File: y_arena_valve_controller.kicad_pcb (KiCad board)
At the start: 2 copper layers, 76.2 x 41.3 mm, 45 parts, among them P1 HEADER_02X12_SMD, SW1 SPST_SLIDE_AS

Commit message: y_arena_valve_board -> y_arena_valve_controller
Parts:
- D1, D11, D13, D15, D17, D3, D5, D7, D9: footprint y_arena_valve_board:SOD-123 -> y_arena_valve_controller:SOD-123
- D10, D12, D14, D16, D18, D2, D4, D6, D8: footprint y_arena_valve_board:LED0805 -> y_arena_valve_controller:LED0805
- FID1, FID2, FID3, FID4: footprint y_arena_valve_board:FIDUCIAL -> y_arena_valve_controller:FIDUCIAL
- MH1, MH2, MH3: footprint y_arena_valve_board:MOUNTING_HOLE_4-40 -> y_arena_valve_controller:MOUNTING_HOLE_4-40
- P1: footprint y_arena_valve_board:HEADER_02x12_SMD -> y_arena_valve_controller:HEADER_02x12_SMD
- R1, R2, R3, R4, R5, R6, R7, R8, R9: footprint y_arena_valve_board:SM0805 -> y_arena_valve_controller:SM0805
- S1, S2, S3, S4, S5, S6, S7, S8, S9: footprint y_arena_valve_board:LEECO_LHDB -> y_arena_valve_controller:LEECO_LHDB
- SW1: footprint y_arena_valve_board:SPST_SLIDE_AS -> y_arena_valve_controller:SPST_SLIDE_AS

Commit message: First draft of schematic
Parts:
- removed P1: HEADER_02X12_SMD, y_arena_valve_controller:HEADER_02x12_SMD
- added C1: 10uF, y_arena_valve_controller:SM0805, F.Cu at (84.9, -20.0)
- added C2: 10uF, y_arena_valve_controller:SM0805, F.Cu at (111.6, -46.6)
- added C3: 0.1uF, power_switches:SM0805, F.Cu at (154.2, -46.6)
- added C4: 0.1uF, power_switches:SM0805, F.Cu at (154.2, -26.4)
- added D19: diode_low_rev_current, valve_with_led:SOD-123, F.Cu at (66.9, -5.98)
- added D20: LED_GRN, valve_with_led:LED0805, F.Cu at (70.8, -5.34)
- added R10: 499, valve_with_led:SM0805, F.Cu at (73.4, -5.38)
- added REG1: CONV_DC_DC_5VIN_12VOUT, y_arena_valve_controller:DC_DC_CONV_SKM10_DKM10, F.Cu at (115.6, 116.8)
- added TEENSY1: TEENSY_4.0, y_arena_valve_controller:TEENSY_4.0, F.Cu at (77.5, 116.8)
- added U1: TLE7230R, power_switches:PG-DSO-36, F.Cu at (144.0, -40.6)
- added U2: TLE7230R, power_switches:PG-DSO-36, F.Cu at (144.0, -20.4)
- D10, D12, D14, D16, D18, D4, D6, D8: footprint y_arena_valve_controller:LED0805 -> valve_with_led:LED0805
- D11, D13, D15, D17, D3, D5, D7, D9: footprint y_arena_valve_controller:SOD-123 -> valve_with_led:SOD-123
- R2, R3, R4, R5, R6, R7, R8, R9: footprint y_arena_valve_controller:SM0805 -> valve_with_led:SM0805
- S1, S2, S3, S4, S5, S6, S7, S8, S9: footprint y_arena_valve_controller:LEECO_LHDB -> valve_with_led:LEECO_LHDB
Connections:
- D10 pad 2: /VALVE_4 -> /VALVE_3
- D12 pad 2: /VALVE_5 -> /VALVE_4
- D14 pad 2: /VALVE_6 -> /VALVE_5
- D16 pad 2: /VALVE_7 -> /VALVE_6
- D18 pad 2: /VALVE_8 -> /VALVE_7
- D2 pad 2: /VALVE_0 -> GND
- D4 pad 2: /VALVE_1 -> /VALVE_0
- D6 pad 2: /VALVE_2 -> /VALVE_1
- D8 pad 2: /VALVE_3 -> /VALVE_2

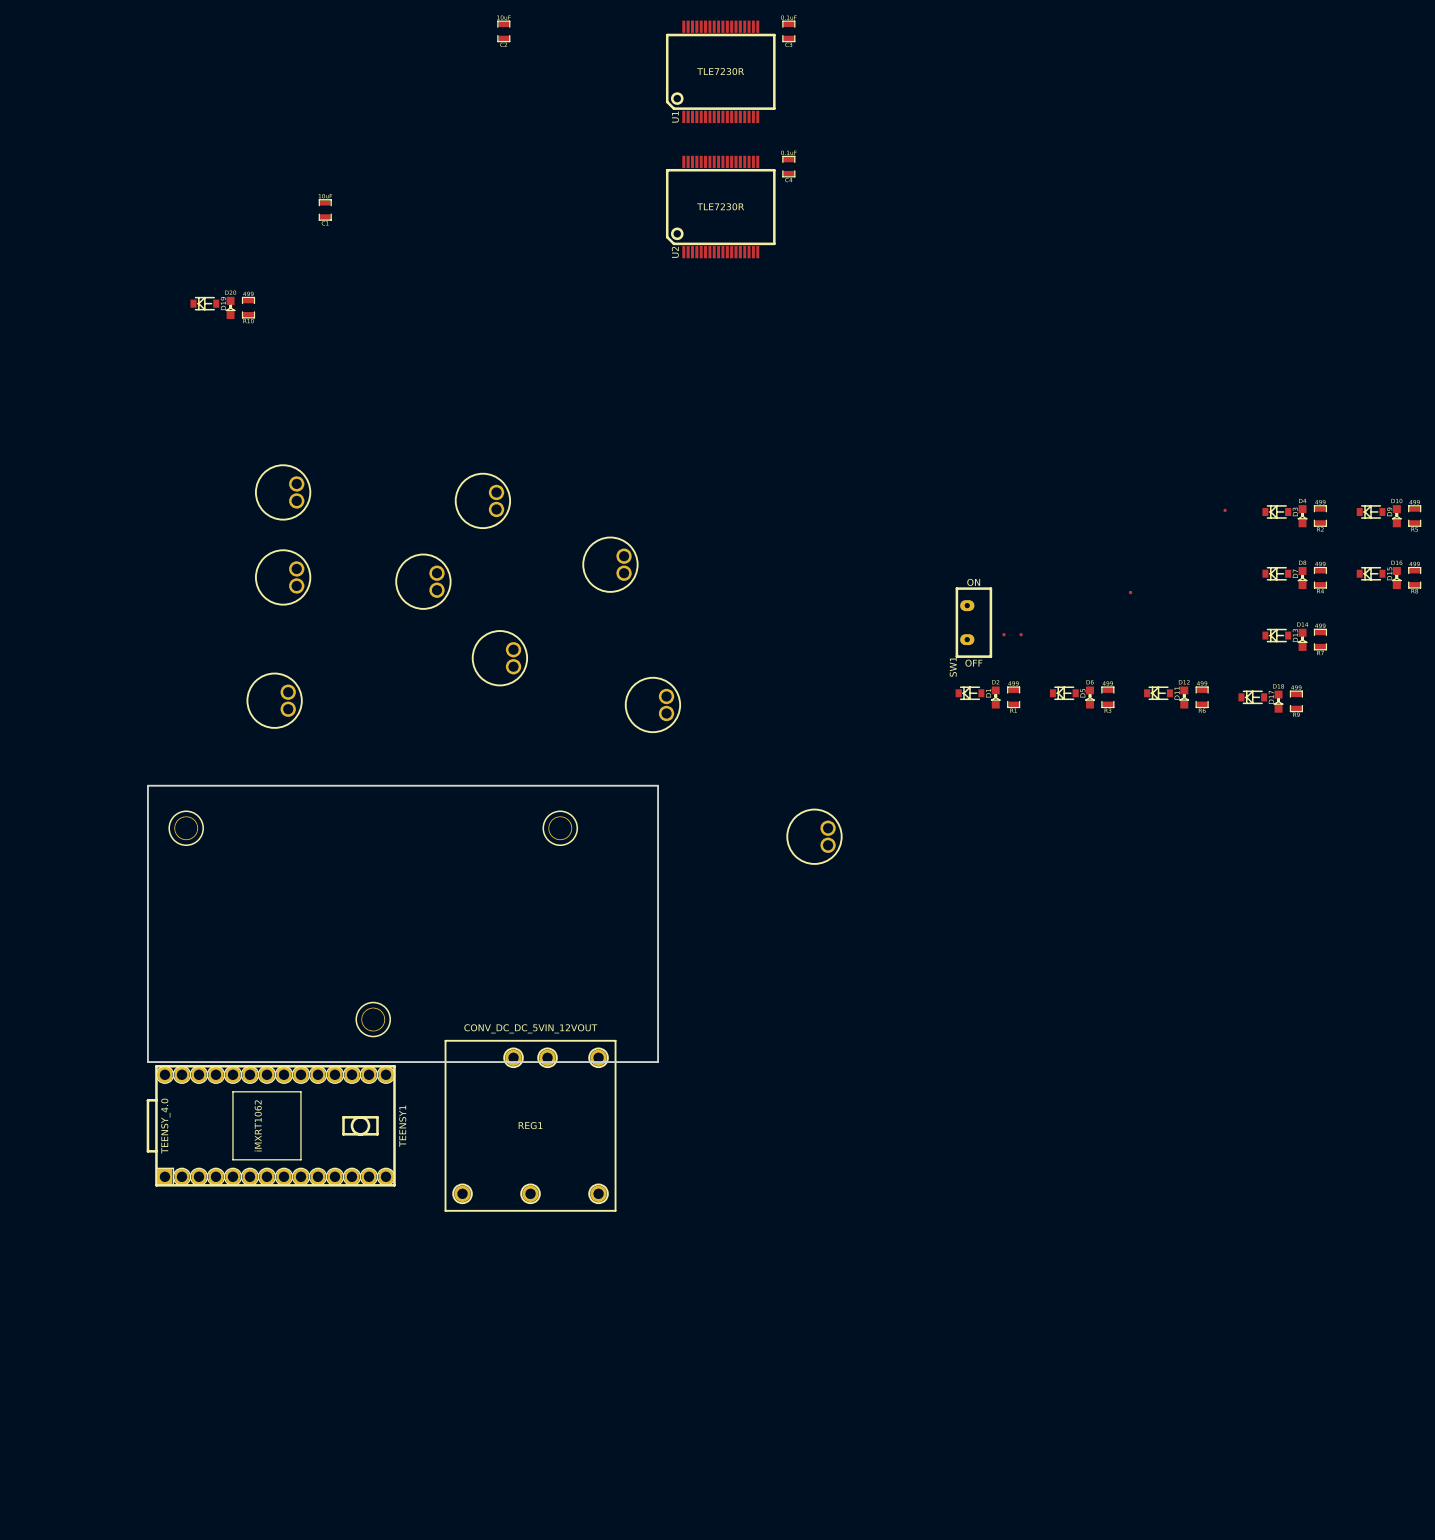
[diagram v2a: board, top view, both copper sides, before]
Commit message: Add phidget
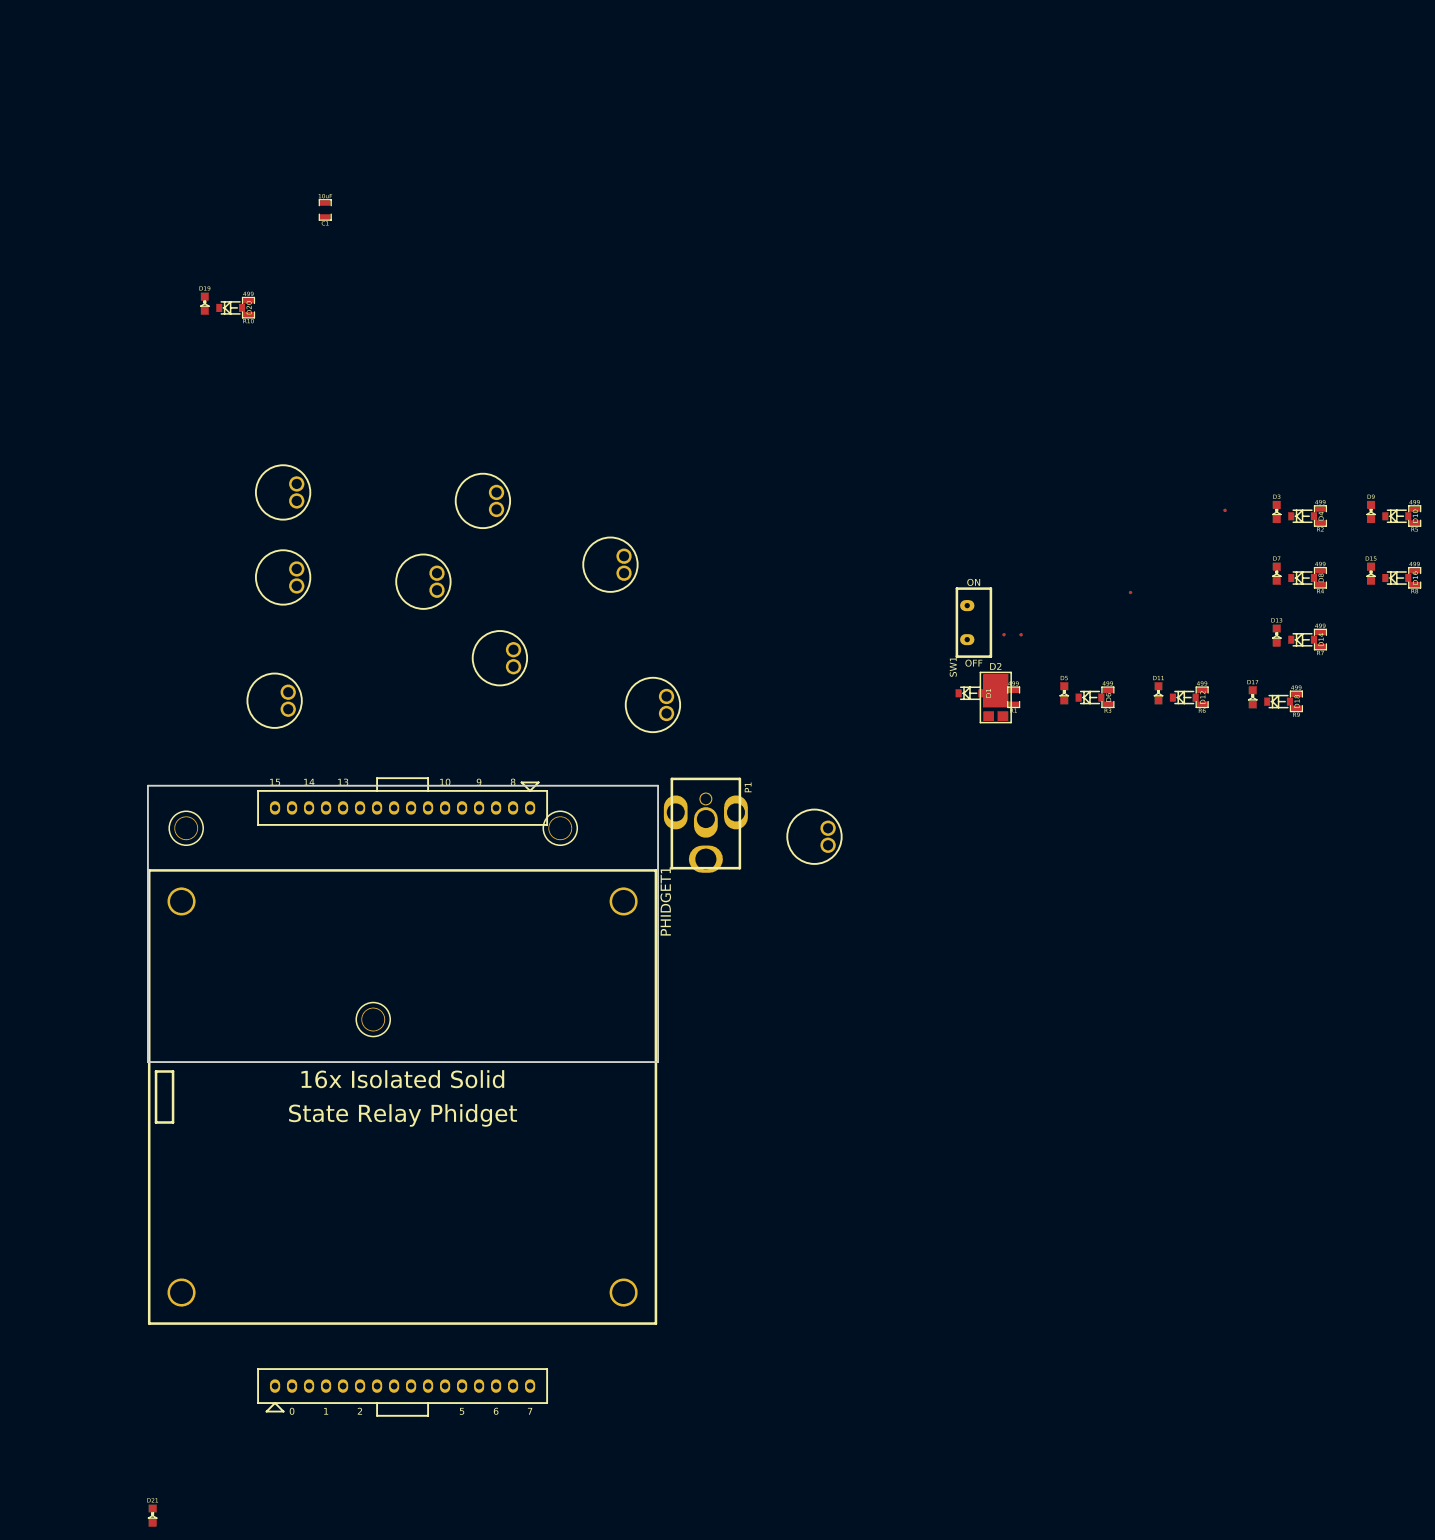
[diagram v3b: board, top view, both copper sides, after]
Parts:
- removed C2: 10uF, y_arena_valve_controller:SM0805
- removed C3, C4: 0.1uF, power_switches:SM0805
- removed REG1: CONV_DC_DC_5VIN_12VOUT, y_arena_valve_controller:DC_DC_CONV_SKM10_DKM10
- removed TEENSY1: TEENSY_4.0, y_arena_valve_controller:TEENSY_4.0
- removed U1, U2: TLE7230R, power_switches:PG-DSO-36
- added D21: LED_GRN, valve_with_led:LED0805, F.Cu at (59.1, 175.1)
- added P1: PWR_JACK_2.1x5.5, y_arena_valve_controller:DCJACK_2PIN_HIGHCURRENT, F.Cu at (141.8, 65.0)
- added PHIDGET1: PHIDGET_RELAY_16X, y_arena_valve_controller:PHIDGET_RELAY_16X, F.Cu at (96.5, 112.5)
- D10, D12, D14, D16, D18, D20, D4, D6, D8: value LED_GRN -> diode_low_rev_current; footprint valve_with_led:LED0805 -> valve_with_led:SOD-123
- D11, D13, D15, D17, D19, D5, D7, D9: value diode_low_rev_current -> LED_GRN; footprint valve_with_led:SOD-123 -> valve_with_led:LED0805
- D2: value LED_GRN -> DIODE_SCHOTTKY_45V_10A; footprint y_arena_valve_controller:LED0805 -> y_arena_valve_controller:CFP15
- D3: value diode_low_rev_current -> LED_GRN; footprint valve_with_led:SOD-123 -> y_arena_valve_controller:LED0805
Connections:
- C1 pad 1: +5V -> VCC
- D10 pad 2: /VALVE_3 -> LED_PWR
- D11 pad 2: LED_PWR -> /VALVE_3
- D12 pad 2: /VALVE_4 -> LED_PWR
- D13 pad 2: LED_PWR -> /VALVE_4
- D14 pad 2: /VALVE_5 -> LED_PWR
- D15 pad 2: LED_PWR -> /VALVE_5
- D16 pad 2: /VALVE_6 -> LED_PWR
- D17 pad 2: LED_PWR -> /VALVE_6
- D18 pad 2: /VALVE_7 -> LED_PWR
- D19 pad 2: LED_PWR -> /VALVE_7
- D2 pad 1: Net-(D2-Pad1) -> VCC
- D2 pad 2: GND -> VAA
- D20 pad 2: /VALVE_8 -> LED_PWR
- D3 pad 2: LED_PWR -> GND
- D4 pad 2: /VALVE_0 -> LED_PWR
- D5 pad 2: LED_PWR -> /VALVE_0
- D6 pad 2: /VALVE_1 -> LED_PWR
- D7 pad 2: LED_PWR -> /VALVE_1
- D8 pad 2: /VALVE_2 -> LED_PWR
- D9 pad 2: LED_PWR -> /VALVE_2
- R1 pad 2: Net-(D2-Pad1) -> Net-(D3-Pad1)
- R10 pad 1: Net-(D19-Pad1) -> Net-(D20-Pad1)
- R10 pad 2: Net-(D20-Pad1) -> Net-(D21-Pad1)
- R2 pad 1: Net-(D3-Pad1) -> Net-(D4-Pad1)
- R2 pad 2: Net-(D4-Pad1) -> Net-(D5-Pad1)
- R3 pad 1: Net-(D5-Pad1) -> Net-(D6-Pad1)
- R3 pad 2: Net-(D6-Pad1) -> Net-(D7-Pad1)
- R4 pad 1: Net-(D7-Pad1) -> Net-(D8-Pad1)
- R4 pad 2: Net-(D8-Pad1) -> Net-(D9-Pad1)
- R5 pad 1: Net-(D9-Pad1) -> Net-(D10-Pad1)
- R5 pad 2: Net-(D10-Pad1) -> Net-(D11-Pad1)
- R6 pad 1: Net-(D11-Pad1) -> Net-(D12-Pad1)
- R6 pad 2: Net-(D12-Pad1) -> Net-(D13-Pad1)
- R7 pad 1: Net-(D13-Pad1) -> Net-(D14-Pad1)
- R7 pad 2: Net-(D14-Pad1) -> Net-(D15-Pad1)
- R8 pad 1: Net-(D15-Pad1) -> Net-(D16-Pad1)
- R8 pad 2: Net-(D16-Pad1) -> Net-(D17-Pad1)
- R9 pad 1: Net-(D17-Pad1) -> Net-(D18-Pad1)
- R9 pad 2: Net-(D18-Pad1) -> Net-(D19-Pad1)
- S1 pad 1: VAA -> VCC
- S2 pad 1: VAA -> VCC
- S3 pad 1: VAA -> VCC
- S4 pad 1: VAA -> VCC
- S5 pad 1: VAA -> VCC
- S6 pad 1: VAA -> VCC
- S7 pad 1: VAA -> VCC
- S8 pad 1: VAA -> VCC
- S9 pad 1: VAA -> VCC
- SW1 pad 1: VAA -> VCC

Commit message: Updated libraries
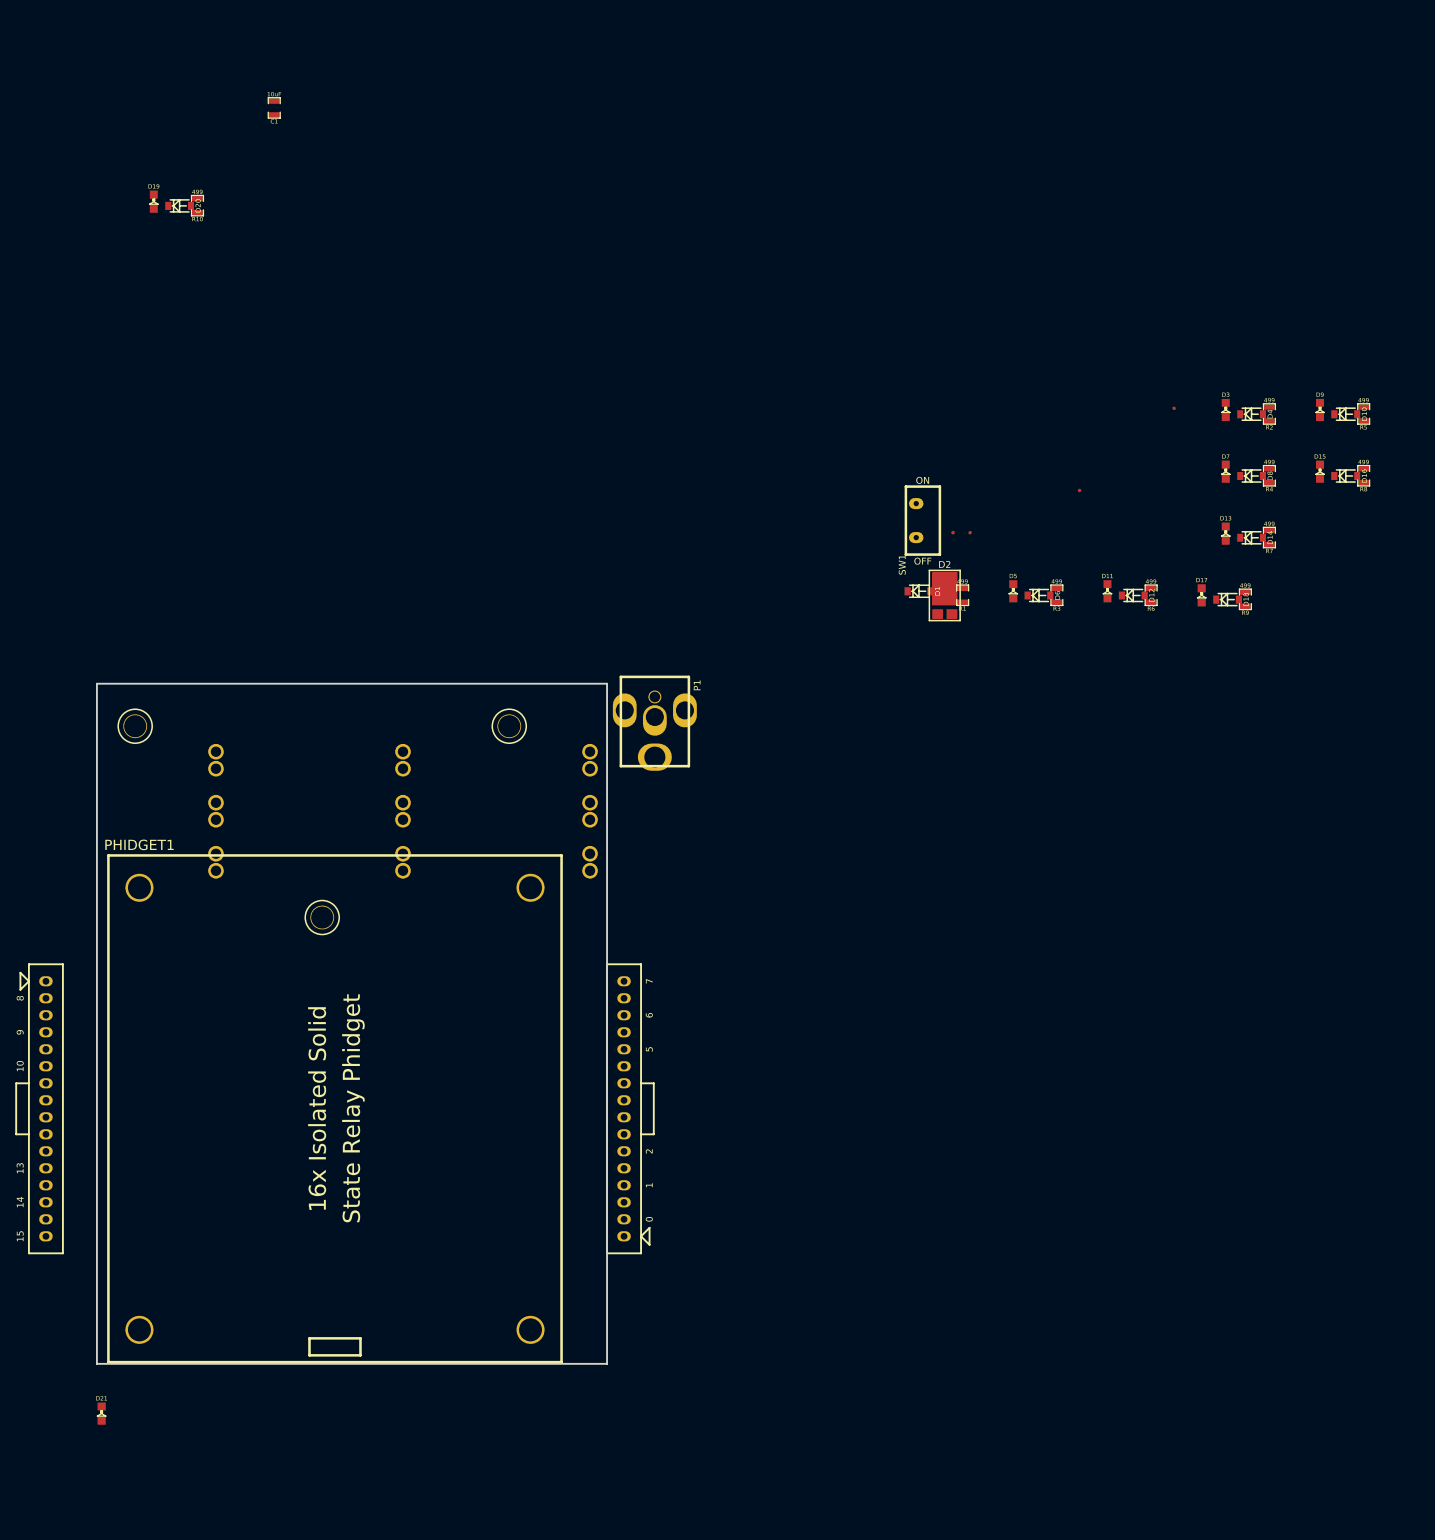
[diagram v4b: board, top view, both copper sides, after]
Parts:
- moved S1 67.6 mm to (68.6, 62.2)
- moved S2 49.1 mm to (68.6, 69.8)
- moved S5 48.4 mm to (96.5, 69.8)
- moved S3 44.2 mm to (68.6, 77.5)
- moved S6 42.2 mm to (96.5, 77.5)
- moved S9 35.8 mm to (124.5, 77.5)
- moved S8 25.6 mm to (124.5, 69.8)
- moved S4 19.3 mm to (96.5, 62.2)
- moved D21 17.0 mm to (51.5, 159.8)
- moved MH1 17.0 mm to (84.5, 85.7)
- moved D10 17.0 mm to (237.4, 10.5)
- moved D13 17.0 mm to (219.4, 28.4)
- moved D14 17.0 mm to (223.3, 29.0)
- moved D15 17.0 mm to (233.5, 19.1)
- moved D16 17.0 mm to (237.4, 19.8)
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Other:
- board size 76.2 x 41.3 mm -> 76.2 x 101.6 mm

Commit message: Finished schematic v1.0
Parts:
- removed D10, D12, D14, D16, D18, D20, D4, D6, D8: diode_low_rev_current, valve_with_led:SOD-123
- removed D11, D13, D15, D17, D19, D21, D5, D7, D9: LED_GRN, valve_with_led:LED0805
- removed D2: DIODE_SCHOTTKY_45V_10A, y_arena_valve_controller:CFP15
- removed D3: LED_GRN, y_arena_valve_controller:LED0805
- removed R1: 499, y_arena_valve_controller:SM0805
- removed R10, R2, R3, R4, R5, R6, R7, R8, R9: 499, valve_with_led:SM0805
- removed SW1: SPST_SLIDE_AS, y_arena_valve_controller:SPST_SLIDE_AS
- D1: value diode_low_rev_current -> DIODE_SCHOTTKY_45V_10A; footprint y_arena_valve_controller:SOD-123 -> y_arena_valve_controller:CFP15
- MH1, MH2, MH3: moved to B.Cu
- P1: value PWR_JACK_2.1x5.5 -> PWR_JACK_2.1x5.5_SMD_VERT; footprint y_arena_valve_controller:DCJACK_2PIN_HIGHCURRENT -> y_arena_valve_controller:DCJACK_3PIN_SMD_VERT
- PHIDGET1: value PHIDGET_RELAY_16X -> PHIDGET_RELAY_16X_COMP; footprint y_arena_valve_controller:PHIDGET_RELAY_16X -> y_arena_valve_controller:PHIDGET_RELAY_16X_COMP; moved to B.Cu
- S1, S2, S3, S4, S5, S6, S7, S8, S9: value LEECO_LHDB -> VAL**; footprint valve_with_led:LEECO_LHDB -> valve:LEECO_LHDB; moved to F.Cu
- moved FID4 189.4 mm to (54.0, 145.4), turned to 180 degrees
- moved C1 175.6 mm to (78.7, 140.3), turned to 90 degrees
- moved FID1 163.8 mm to (54.0, 54.0), turned to 180 degrees
- moved FID3 129.9 mm to (122.6, 145.4), turned to 180 degrees
- moved D1 114.1 mm to (88.3, 112.8)
- moved P1 91.5 mm to (88.3, 128.9)
- moved MH3 64.1 mm to (120.7, 56.5), turned to 180 degrees
- moved FID2 64.1 mm to (122.6, 54.0), turned to 180 degrees
- moved MH2 47.6 mm to (64.8, 56.5), turned to 180 degrees
- moved S3 22.5 mm to (52.7, 61.6)
- moved S6 22.5 mm to (80.6, 61.6)
- moved S9 22.5 mm to (108.6, 61.6)
- moved S1 21.6 mm to (52.7, 76.8)
- moved S4 21.6 mm to (80.6, 76.8)
- moved S7 21.6 mm to (108.6, 76.8)
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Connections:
- D1 pad 1: Net-(D1-Pad1) -> VCC
- D1 pad 2: LED_PWR -> VAA
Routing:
- net VCC: track 0.00 -> 183.5 mm
- net GND: track 0.00 -> 155.5 mm
- net /VALVE_2: track 0.00 -> 70.0 mm
- net /VALVE_1: track 0.00 -> 69.6 mm
- net /VALVE_7: track 0.00 -> 62.2 mm
- net /VALVE_6: track 0.00 -> 61.1 mm
- net /VALVE_0: track 0.00 -> 61.1 mm
- net /VALVE_5: track 0.00 -> 58.5 mm
- net /VALVE_4: track 0.00 -> 54.7 mm, vias 0 -> 1
- net /VALVE_3: track 0.00 -> 52.1 mm, vias 0 -> 1
- net /VALVE_8: track 0.00 -> 44.3 mm
- net VAA: track 0.00 -> 8.08 mm
- added copper zone on F.Cu, net VCC
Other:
- board size 76.2 x 101.6 mm -> 74.9 x 97.8 mm
- net class SUPERPOWER added: clearance 0.1016, trace_width 0.8128, via_dia 0.889, via_drill 0.635
- board text added: "2.1x5.5 Center + +12VDC"
- board text added: "y_arena_valve_controller Janelia Research Campus 07/20/2020 VER 1.0"

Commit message: Finished ver 1.0
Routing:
- added copper zone on B.Cu, net GND
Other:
- board text added: "y_arena_valve_controller Janelia Research Campus 07/20/2020 ver 1.0"
- board text removed: "y_arena_valve_controller Janelia Research Campus 07/20/2020 VER 1.0"
